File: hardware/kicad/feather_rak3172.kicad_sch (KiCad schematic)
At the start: 49 parts, among them J1 Pin Header, J2 Pin Header, J3 USB_C_Receptacle_USB2.0, J5 SWD, J6 JST-2PH, Q1 DMG341, SW1 RESET, SW2 BOOT, U1 RAK3172, U2 CH340E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

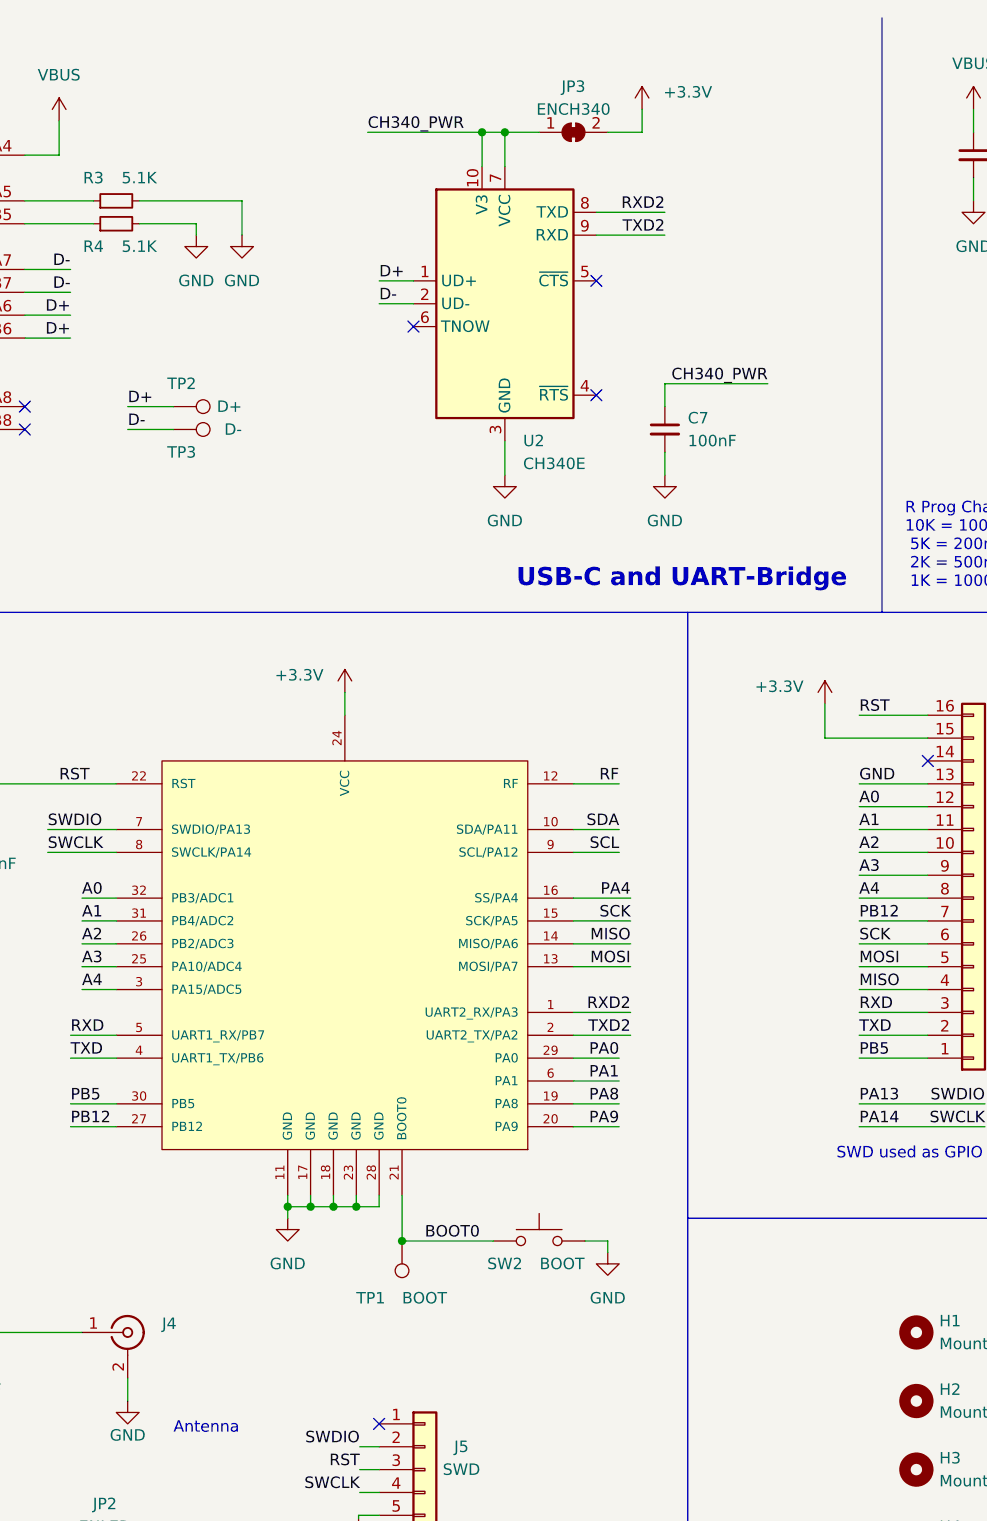
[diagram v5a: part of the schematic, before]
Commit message: add solder jump for txd and rxd, minor silkscreen changes
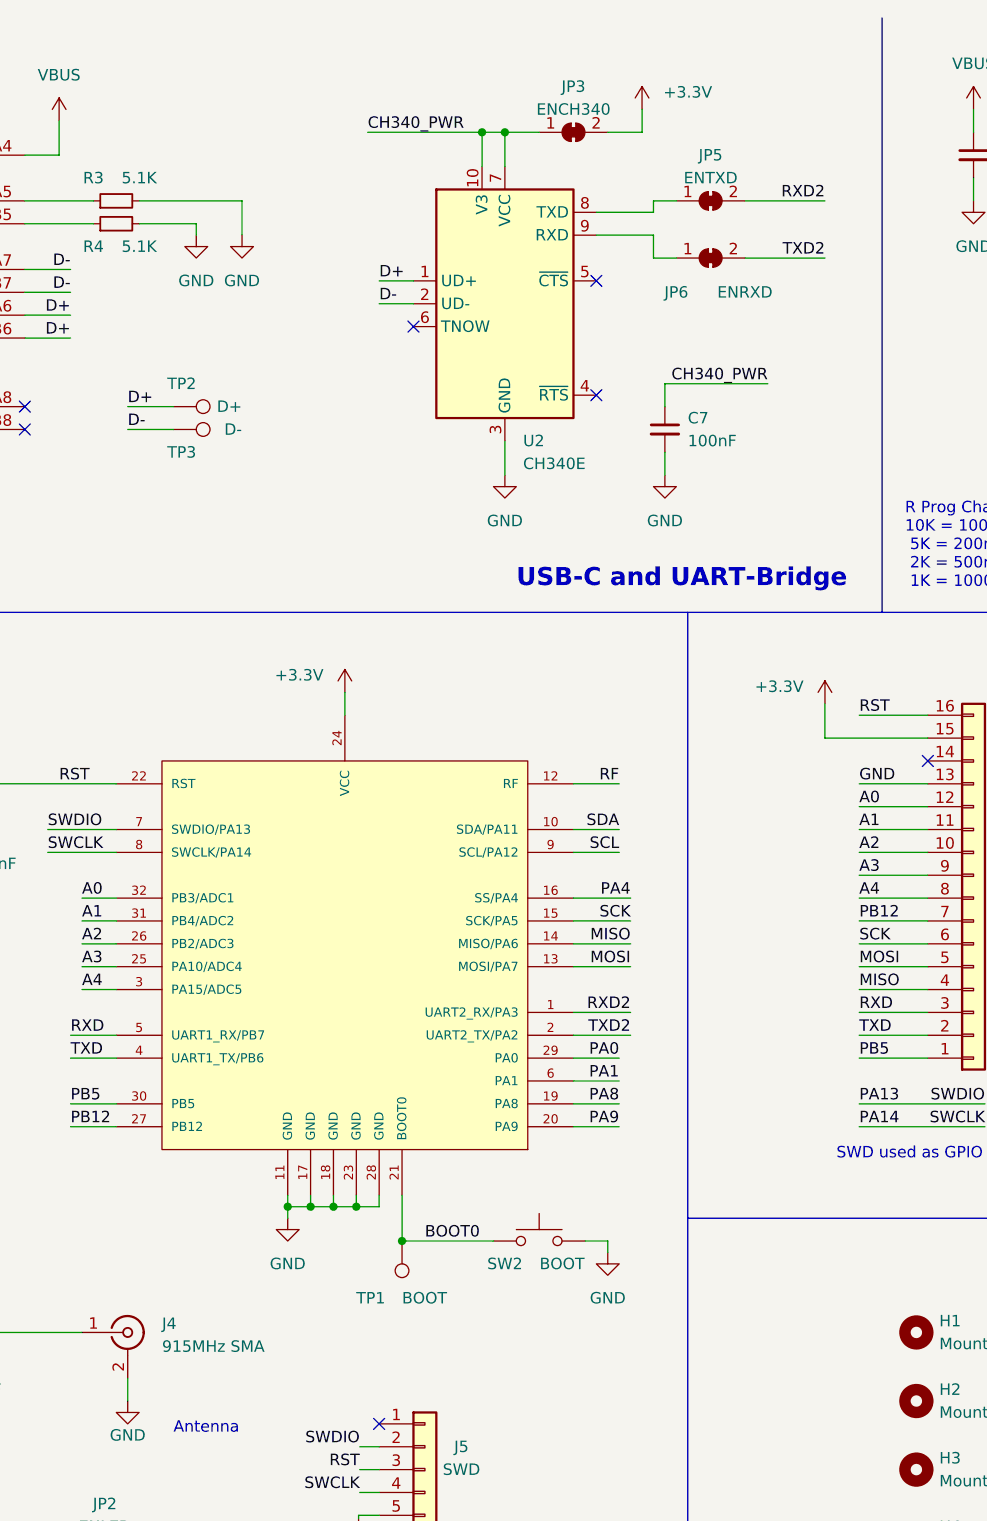
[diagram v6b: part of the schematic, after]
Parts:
- added JP5: ENTXD, Jumper:SolderJumper-2_P1.3mm_Bridged_RoundedPad1.0x1.5mm, symbol Jumper:SolderJumper_2_Bridged
- added JP6: ENRXD, Jumper:SolderJumper-2_P1.3mm_Bridged_RoundedPad1.0x1.5mm, symbol Jumper:SolderJumper_2_Bridged
- J4: value (none) -> 915MHz SMA; footprint (none) -> Teapot:SMA_HJTech_023
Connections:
- net RXD2: now also JP5.2 (B); no longer U2.8 (TXD)
- net TXD2: now also JP6.2 (B); no longer U2.9 (RXD)
- new net: JP6.1 (A), U2.9 (RXD)
- new net: JP5.1 (A), U2.8 (TXD)
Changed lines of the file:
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@@
   (title_block
     (title "Feather RAK3172")
-    (date "2023-02-10")
-    (rev "7")
+    (date "2023-02-21")
+    (rev "8")
     (company "Teapot Laboratories")
   )
@@
     (stroke (width 0) (type default) (color 0 0 0 0))
   )
+  (wire (pts (xy 125.73 33.02) (xy 134.62 33.02))
+    (stroke (width 0) (type default) (color 0 0 0 0))
+  )
   (wire (pts (xy 29.21 184.15) (xy 22.86 184.15))
     (stroke (width 0) (type default) (color 0 0 0 0))
@@
     (stroke (width 0) (type default) (color 0 0 0 0))
   )
+  (wire (pts (xy 115.57 33.02) (xy 118.11 33.02))
+    (stroke (width 0) (type default) (color 0 0 0 0))
+  )
+  (wire (pts (xy 115.57 34.29) (xy 115.57 33.02))
+    (stroke (width 0) (type default) (color 0 0 0 0))
+  )
   (wire (pts (xy 138.43 118.11) (xy 146.05 118.11))
     (stroke (width 0) (type default) (color 0 0 0 0))
@@
     (stroke (width 0) (type default) (color 0 0 0 0))
   )
+  (wire (pts (xy 109.22 34.29) (xy 115.57 34.29))
+    (stroke (width 0) (type default) (color 0 0 0 0))
+  )
   (wire (pts (xy 116.84 60.96) (xy 116.84 63.5))
     (stroke (width 0) (type default) (color 0 0 0 0))
@@
     (stroke (width 0) (type default) (color 0 0 0 0))
   )
-  (wire (pts (xy 109.22 34.29) (xy 116.84 34.29))
-    (stroke (width 0) (type default) (color 0 0 0 0))
-  )
   (wire (pts (xy 198.755 46.99) (xy 193.04 46.99))
     (stroke (width 0) (type default) (color 0 0 0 0))
@@
     (stroke (width 0) (type default) (color 0 0 0 0))
   )
-  (wire (pts (xy 109.22 36.83) (xy 116.84 36.83))
-    (stroke (width 0) (type default) (color 0 0 0 0))
-  )
   (wire (pts (xy 179.07 115.57) (xy 173.99 115.57))
     (stroke (width 0) (type default) (color 0 0 0 0))
@@
     (stroke (width 0) (type default) (color 0 0 0 0))
   )
+  (wire (pts (xy 125.73 39.37) (xy 134.62 39.37))
+    (stroke (width 0) (type default) (color 0 0 0 0))
+  )
   (wire (pts (xy 265.43 36.83) (xy 265.43 44.45))
     (stroke (width 0) (type default) (color 0 0 0 0))
@@
     (stroke (width 0) (type default) (color 0 0 0 0))
   )
+  (wire (pts (xy 115.57 39.37) (xy 118.11 39.37))
+    (stroke (width 0) (type default) (color 0 0 0 0))
+  )
   (wire (pts (xy 36.83 184.15) (xy 41.91 184.15))
     (stroke (width 0) (type default) (color 0 0 0 0))
@@
   )
   (wire (pts (xy 57.15 163.83) (xy 57.15 166.37))
+    (stroke (width 0) (type default) (color 0 0 0 0))
+  )
+  (wire (pts (xy 109.22 36.83) (xy 115.57 36.83))
+    (stroke (width 0) (type default) (color 0 0 0 0))
+  )
+  (wire (pts (xy 115.57 36.83) (xy 115.57 39.37))
     (stroke (width 0) (type default) (color 0 0 0 0))
   )
@@
     (effects (font (size 1.27 1.27)) (justify left bottom))
   )
-  (label "TXD2" (at 116.84 36.83 180)
+  (label "TXD2" (at 134.62 39.37 180)
     (effects (font (size 1.27 1.27)) (justify right bottom))
   )
@@
     (effects (font (size 1.27 1.27)) (justify right bottom))
   )
-  (label "RXD2" (at 116.84 34.29 180)
+  (label "RXD2" (at 134.62 33.02 180)
     (effects (font (size 1.27 1.27)) (justify right bottom))
   )
@@
     )
     (pin "1")
+  )
+  (symbol (lib_id "Jumper:SolderJumper_2_Bridged") (at 121.92 39.37 0) (unit 1)
+    (in_bom yes) (on_board yes)
+    (property "Reference" "JP6" (id 0) (at 118.11 43.18 0))
+    (property "Value" "ENRXD" (id 1) (at 125.73 43.18 0))
+    (property "Footprint" "Jumper:SolderJumper-2_P1.3mm_Bridged_RoundedPad1.0x1.5mm" (id 2) (at 121.92 39.37 0)
+      (effects (font (size 1.27 1.27)) hide)
+    )
+    (property "Datasheet" "~" (id 3) (at 121.92 39.37 0)
+      (effects (font (size 1.27 1.27)) hide)
+    )
+    (pin "1")
+    (pin "2")
   )
   (symbol (lib_id "Device:C_Small") (at 116.84 58.42 0) (unit 1)
@@
       (effects (font (size 1.27 1.27)) (justify left))
     )
-    (property "Value" "" (id 1) (at 60.96 160.3131 0)
-      (effects (font (size 1.27 1.27)) (justify left))
-    )
-    (property "Footprint" "" (id 2) (at 57.15 158.75 0)
+    (property "Value" "915MHz SMA" (id 1) (at 60.96 160.3131 0)
+      (effects (font (size 1.27 1.27)) (justify left))
+    )
+    (property "Footprint" "Teapot:SMA_HJTech_023" (id 2) (at 57.15 158.75 0)
       (effects (font (size 1.27 1.27)) hide)
     )
@@
     (pin "1")
   )
+  (symbol (lib_id "Jumper:SolderJumper_2_Bridged") (at 121.92 33.02 0) (unit 1)
+    (in_bom yes) (on_board yes)
+    (property "Reference" "JP5" (id 0) (at 121.92 27.94 0))
+    (property "Value" "ENTXD" (id 1) (at 121.92 30.48 0))
+    (property "Footprint" "Jumper:SolderJumper-2_P1.3mm_Bridged_RoundedPad1.0x1.5mm" (id 2) (at 121.92 33.02 0)
+      (effects (font (size 1.27 1.27)) hide)
+    )
+    (property "Datasheet" "~" (id 3) (at 121.92 33.02 0)
+      (effects (font (size 1.27 1.27)) hide)
+    )
+    (pin "1")
+    (pin "2")
+  )
   (symbol (lib_id "power:GND") (at 161.29 55.88 0) (unit 1)
     (in_bom yes) (on_board yes) (fields_autoplaced)
@@
       (reference "JP4") (unit 1) (value "ENBATTMON") (footprint "Jumper:SolderJumper-2_P1.3mm_Bridged_RoundedPad1.0x1.5mm")
     )
+    (path "/f853e4a3-ea4a-487b-885f-c7b9652dae7b"
+      (reference "JP5") (unit 1) (value "ENTXD") (footprint "Jumper:SolderJumper-2_P1.3mm_Bridged_RoundedPad1.0x1.5mm")
+    )
+    (path "/2abb28ca-027d-43e0-9099-5a35e98674be"
+      (reference "JP6") (unit 1) (value "ENRXD") (footprint "Jumper:SolderJumper-2_P1.3mm_Bridged_RoundedPad1.0x1.5mm")
+    )
     (path "/2f732801-c0be-4b76-a61d-002040a3c720"
